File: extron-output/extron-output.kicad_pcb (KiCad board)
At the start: 2 copper layers, 92 x 37 mm, 12 parts, among them J1 SCART-F, J10 Conn_01x01, J11 Conn_01x01, J2 RED, J3 GREEN, J4 BLUE, J5 SYNC, J6 PHOENIX, J8 Conn_01x01, J9 Conn_01x01, SW1 SW_SPDT

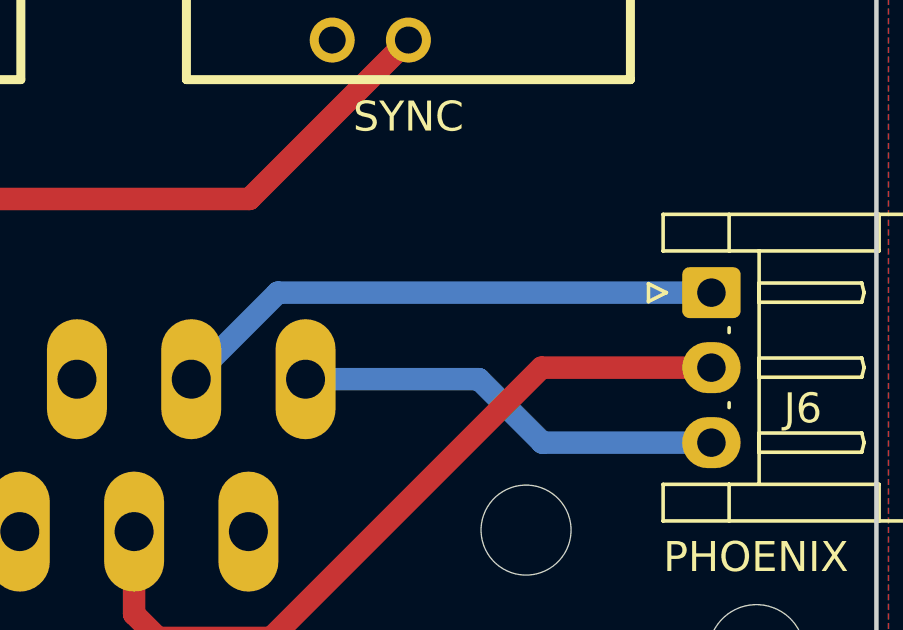
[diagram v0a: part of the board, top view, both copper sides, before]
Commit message: Forgot to reflow the ground planes after making adjustments
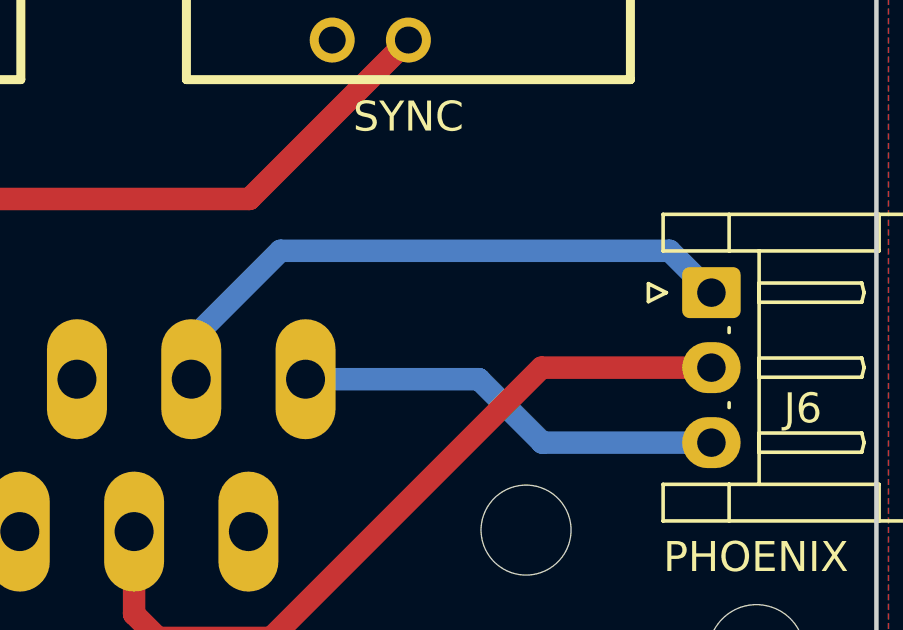
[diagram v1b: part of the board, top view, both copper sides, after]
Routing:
- net Net-(J1-Pad3): track 18.5 -> 20.5 mm
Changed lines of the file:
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@@
     (thickness 1.6)
     (drawings 7)
-    (tracks 35)
+    (tracks 37)
     (zones 0)
     (modules 12)
@@
   )
   (setup
-    (last_trace_width 0.75)
+    (last_trace_width 0.254)
     (user_trace_width 0.5)
     (user_trace_width 0.75)
@@
   (segment (start 148.971 99.8855) (end 154.7495 99.8855) (width 0.75) (layer B.Cu) (net 6))
   (segment (start 154.7495 99.8855) (end 156.864 102) (width 0.75) (layer B.Cu) (net 6))
-  (segment (start 148.0465 97) (end 162.5 97) (width 0.75) (layer B.Cu) (net 11))
-  (segment (start 145.161 99.8855) (end 148.0465 97) (width 0.75) (layer B.Cu) (net 11))
+  (segment (start 161.1056 95.6056) (end 162.5 97) (width 0.75) (layer B.Cu) (net 11))
+  (segment (start 148.1328 95.6056) (end 161.1056 95.6056) (width 0.75) (layer B.Cu) (net 11))
+  (segment (start 145.161 99.8855) (end 145.161 98.5774) (width 0.75) (layer B.Cu) (net 11))
+  (segment (start 145.161 98.5774) (end 148.1328 95.6056) (width 0.75) (layer B.Cu) (net 11))
   (segment (start 114.681 99.8855) (end 114.0984 99.8855) (width 0.75) (layer B.Cu) (net 12))
   (segment (start 111.5027 95.7072) (end 102.6668 95.7072) (width 0.75) (layer B.Cu) (net 12))

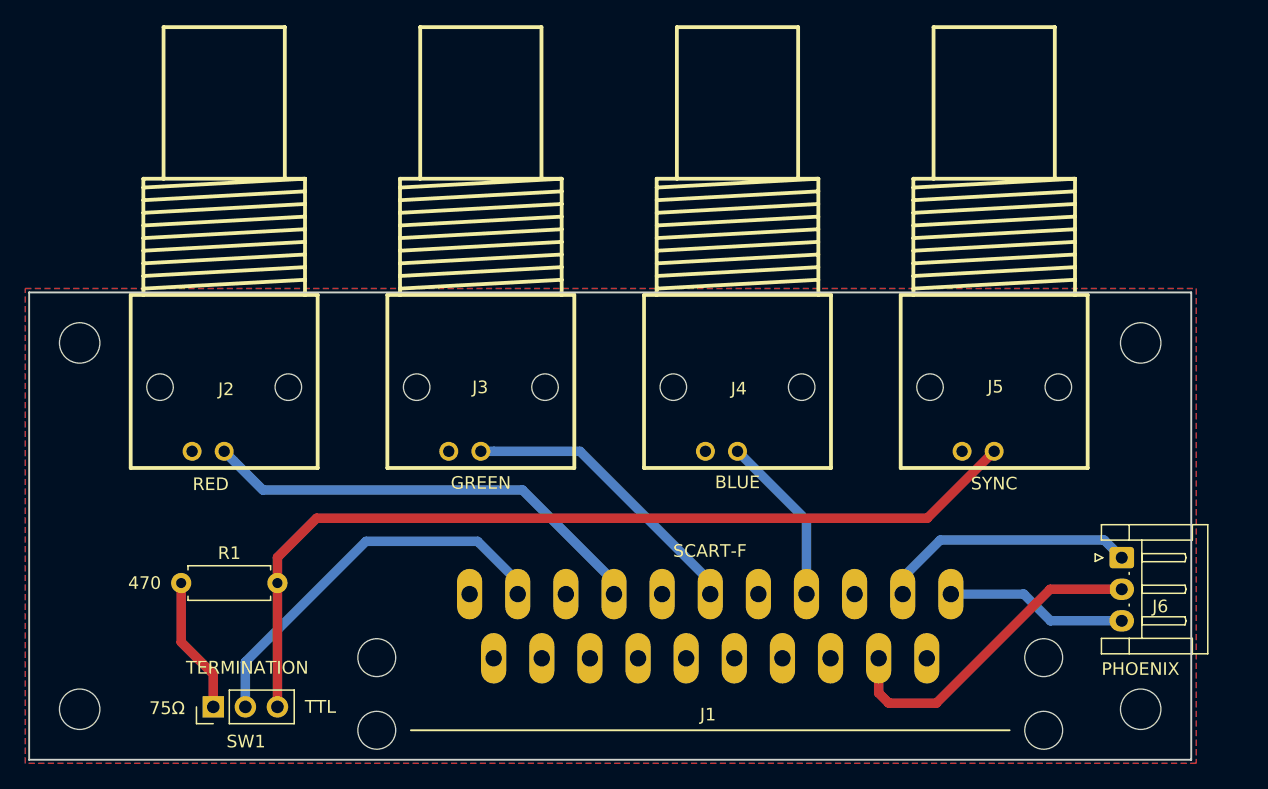
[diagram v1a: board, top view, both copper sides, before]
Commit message: Update extron output board to use combined RCA (v2.1)
Small fixes for extron input as well (v2.1)
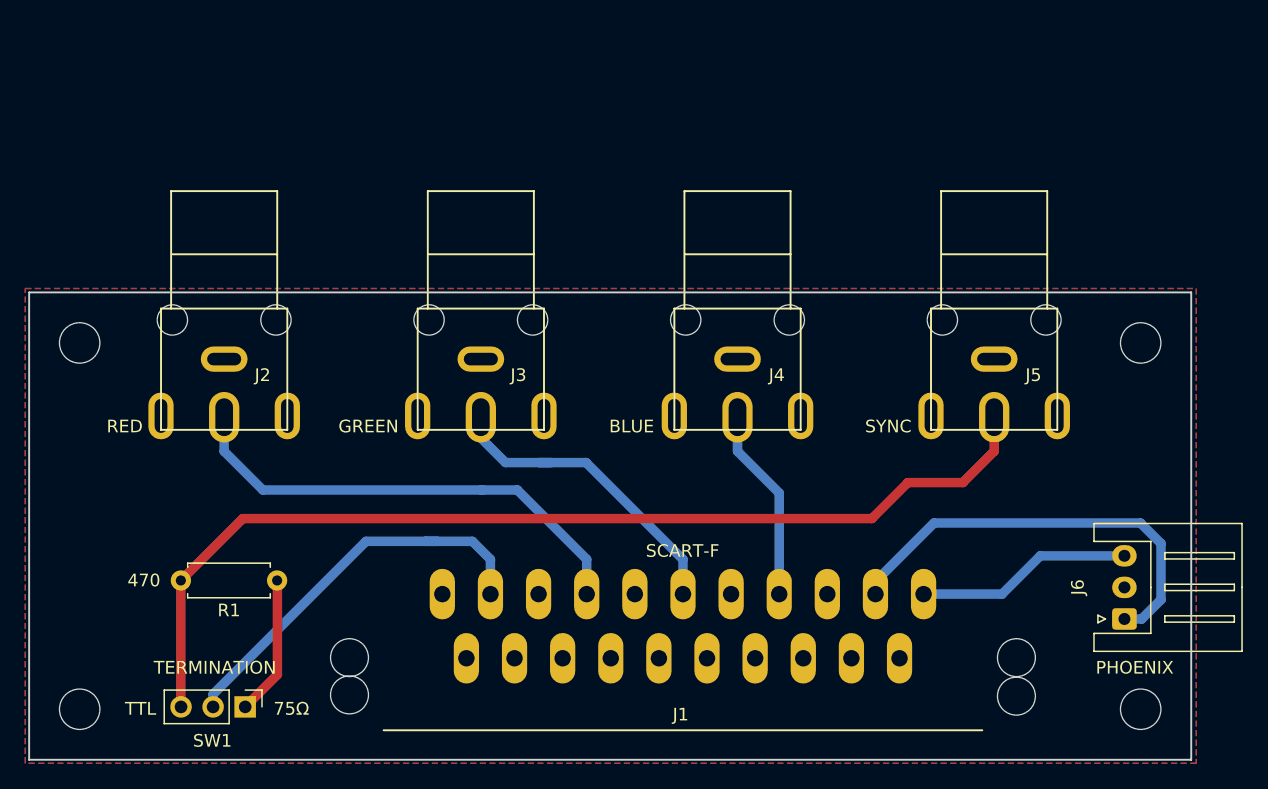
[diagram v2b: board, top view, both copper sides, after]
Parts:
- added REF**: OSHW-Logo_7.5x8mm_SilkScreen, Symbol:OSHW-Logo_7.5x8mm_SilkScreen, B.Cu at (124.5, 92.7)
- added REF**: KiCad-Logo_5mm_SilkScreen, Symbol:KiCad-Logo_5mm_SilkScreen, B.Cu at (111.8, 92.7)
- J2, J3, J4, J5: footprint extron-output:BNC_90 -> extron-output:rca_combined
- J6: footprint Connector_JST:JST_EH_S03B-EH_1x03_P2.50mm_Horizontal -> Connector_JST:JST_XH_S3B-XH-A_1x03_P2.50mm_Horizontal
- moved R1 7.60 mm to (95.6, 98.8), turned to 180 degrees
- moved J2 5.08 mm to (91.4, 81.3)
- moved J3 5.08 mm to (111.8, 81.3)
- moved J4 5.08 mm to (132.1, 81.3)
- moved J5 5.08 mm to (152.4, 81.3)
- moved J6 4.86 mm to (162.7, 101.9), turned to 90 degrees
- moved SW1 2.53 mm to (93.1, 108.8), turned to 270 degrees
- moved J1 2.16 mm to (127.8, 105.0)
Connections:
- J1 pad 4: Net-(J1-Pad4) -> GND
- J2 pad 1: RED -> GND
- J2 pad 2: GND -> RED
- J3 pad 1: GREEN -> GND
- J3 pad 2: GND -> GREEN
- J4 pad 1: BLUE -> GND
- J4 pad 2: GND -> BLUE
- J5 pad 1: SYNC -> GND
- J5 pad 2: GND -> SYNC
- J6 pad 2: Net-(J1-Pad4) -> GND
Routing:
- net Net-(J1-Pad4): track 26.1 -> 0.00 mm
- net Net-(J1-Pad3): track 20.5 -> 34.2 mm
- net SYNC: track 72.1 -> 81.3 mm
- net Net-(J1-Pad1): track 14.4 -> 17.2 mm
- net GREEN: track 23.4 -> 25.3 mm
- net BLUE: track 13.6 -> 15.4 mm
- net RED: track 36.1 -> 37.8 mm
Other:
- board text added: "https://github.com/rattboi/extron-scart-adapter/"
- board text added: "v2.1"
